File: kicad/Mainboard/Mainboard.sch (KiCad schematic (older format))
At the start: 0 parts

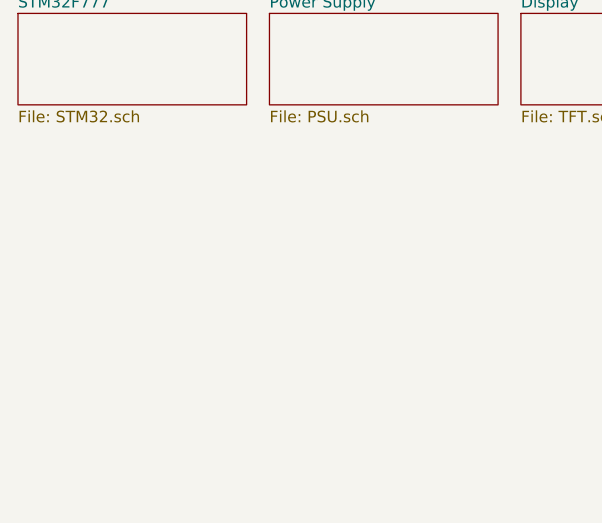
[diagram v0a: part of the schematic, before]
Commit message: added Jumper cable connections description -> moved "M17" and "TR-9" labels -> added label "v 2.0" -> plotted PDF
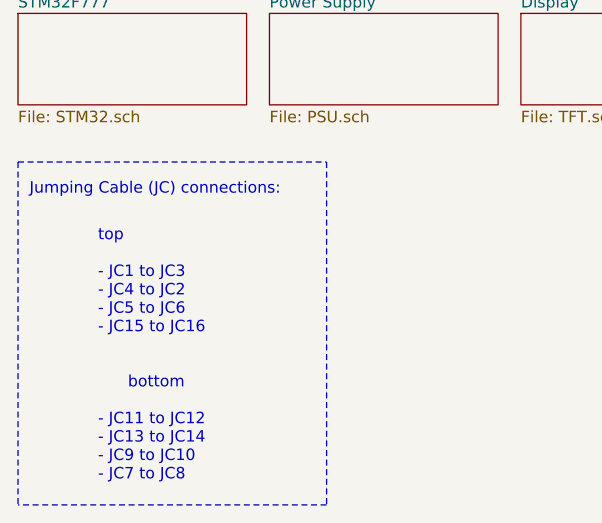
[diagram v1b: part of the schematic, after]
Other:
- note added: "Jumping Cable (JC) connections:\n"
- note added: "top\n\n- JC1 to JC3\n- JC4 to JC2\n- JC5 to JC6\n- JC15 to JC16\n\n\n bottom\n\n- JC11 to JC12\n- JC13 to JC14\n- JC9 to JC10\n- JC7 to JC8"
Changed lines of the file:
@@
 F1 "Modules.sch" 50
 $EndSheet
+Wire Notes Line width 12
+	750  1500 2100 1500
+Wire Notes Line width 12
+	2100 3000 750  3000
+Text Notes 800  1650 0    50   ~ 0
+Jumping Cable (JC) connections:\n
+Text Notes 1100 2900 0    50   ~ 0
+      top\n\n- JC1 to JC3\n- JC4 to JC2\n- JC5 to JC6\n- JC15 to JC16\n\n\n      bottom\n\n- JC11 to JC12\n- JC13 to JC14\n- JC9 to JC10\n- JC7 to JC8
+Wire Notes Line width 12
+	2100 1500 2100 3000
+Wire Notes Line width 12
+	750  1500 750  3000
 $EndSCHEMATC
